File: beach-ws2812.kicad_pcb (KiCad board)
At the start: 4 copper layers, 260 x 120 mm, 24 parts, among them CON101 BARREL_JACK, P101 CONN_01X03, SW101 Pushbutton, SW102 Pushbutton, U101 STM32F103C(8-B)Tx, U102 LM1117-3.3, U103 MAX811, X101 8MHz

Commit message: Finished routing with only 1 random placed LED.
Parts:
- moved C201 7.02 mm to (25.0, 29.5), turned to 270 degrees
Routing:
- net LEDDATA: track 2.40 -> 240.8 mm, vias 1 -> 3
- net +3V3: track 120.6 -> 173.3 mm
- net GND: track 87.2 -> 128.5 mm, vias 11 -> 12
- net +5V: track 34.0 -> 41.4 mm, vias 1 -> 2
- net Net-(R101-Pad1): track 0.00 -> 3.90 mm
- net Net-(C102-Pad1): track 16.6 -> 17.7 mm

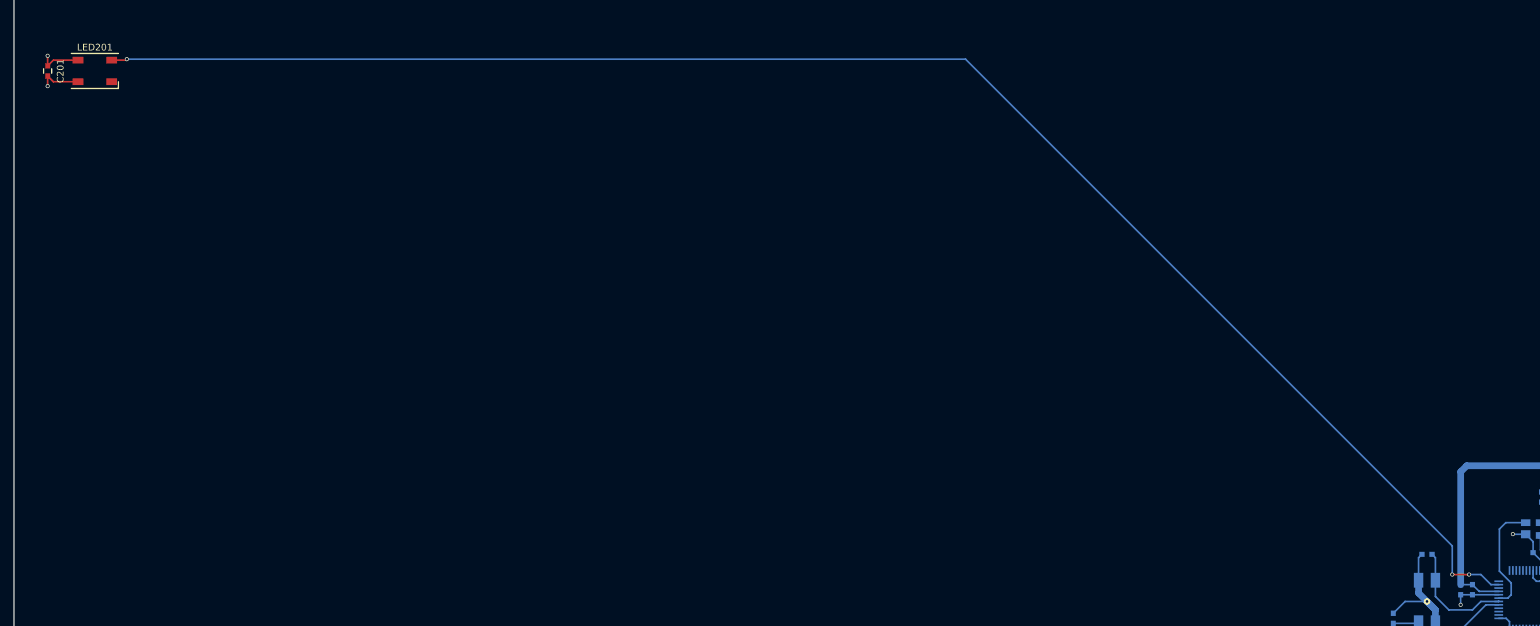
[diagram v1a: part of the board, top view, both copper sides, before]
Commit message: Routed to first LED final position.
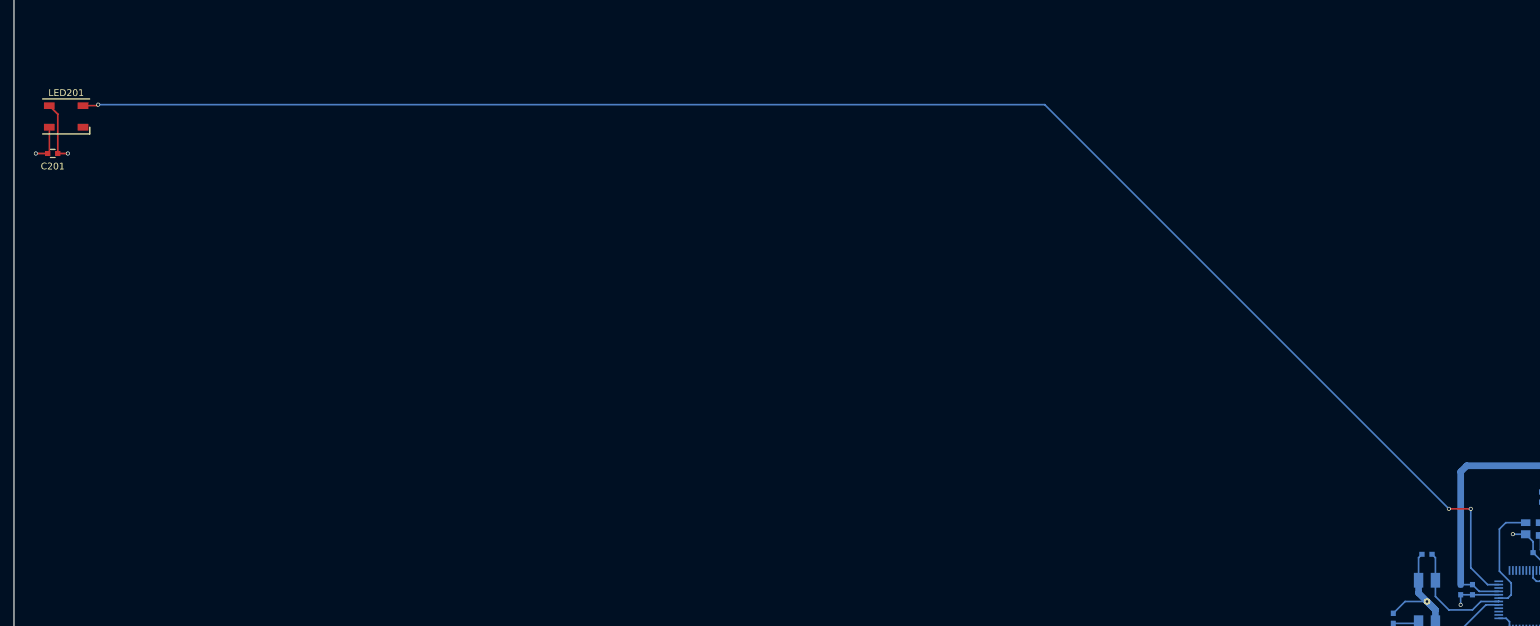
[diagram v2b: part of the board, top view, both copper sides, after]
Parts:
- added G***: LOGO, beach-ws2812:leds, F.Cu at (153.8, 78.5)
- moved C201 12.3 mm to (25.8, 41.8), turned to 180 degrees
- moved LED201 7.98 mm to (27.8, 36.2)
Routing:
- net LEDDATA: track 240.8 -> 244.9 mm
- net +5V: track 41.4 -> 43.9 mm
- net (no net): track 0.00 -> 2.00 mm
- net GND: track 128.5 -> 127.9 mm

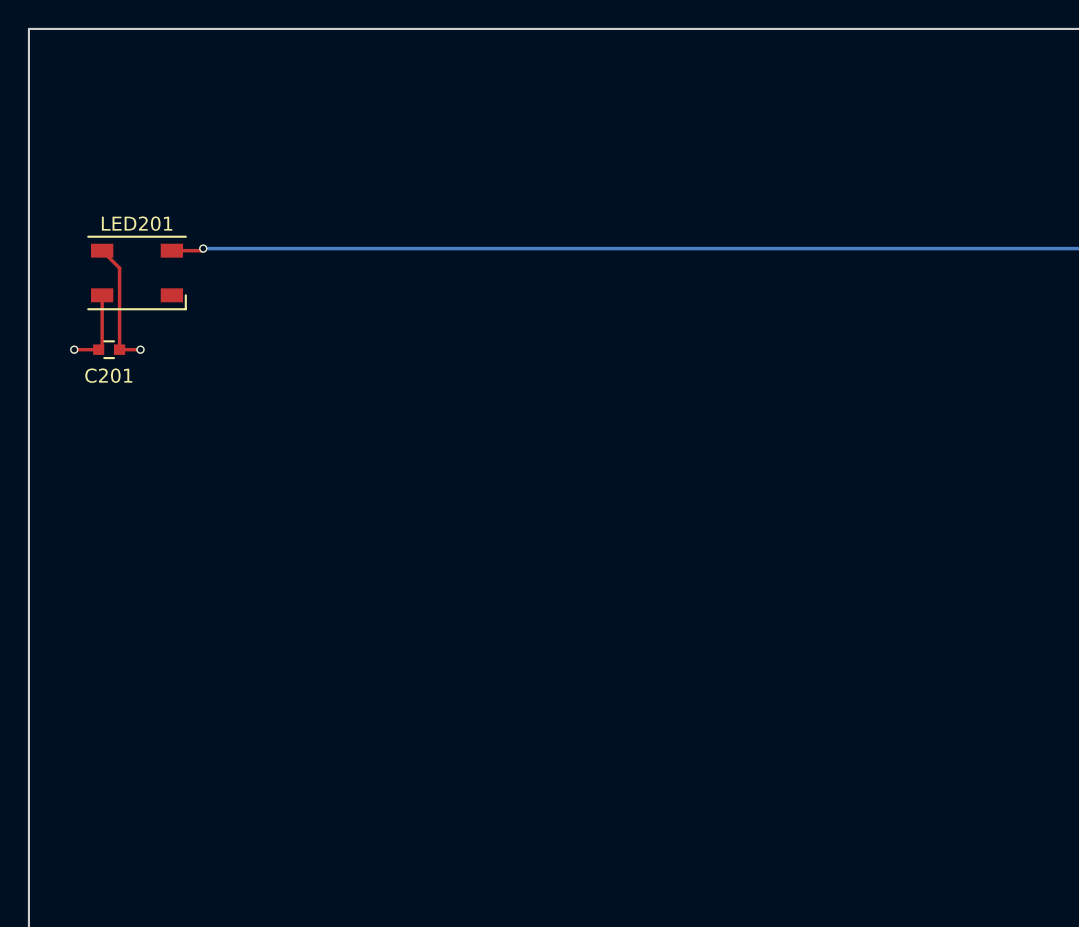
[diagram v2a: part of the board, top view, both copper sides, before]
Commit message: Now with 16 LEDs placed.
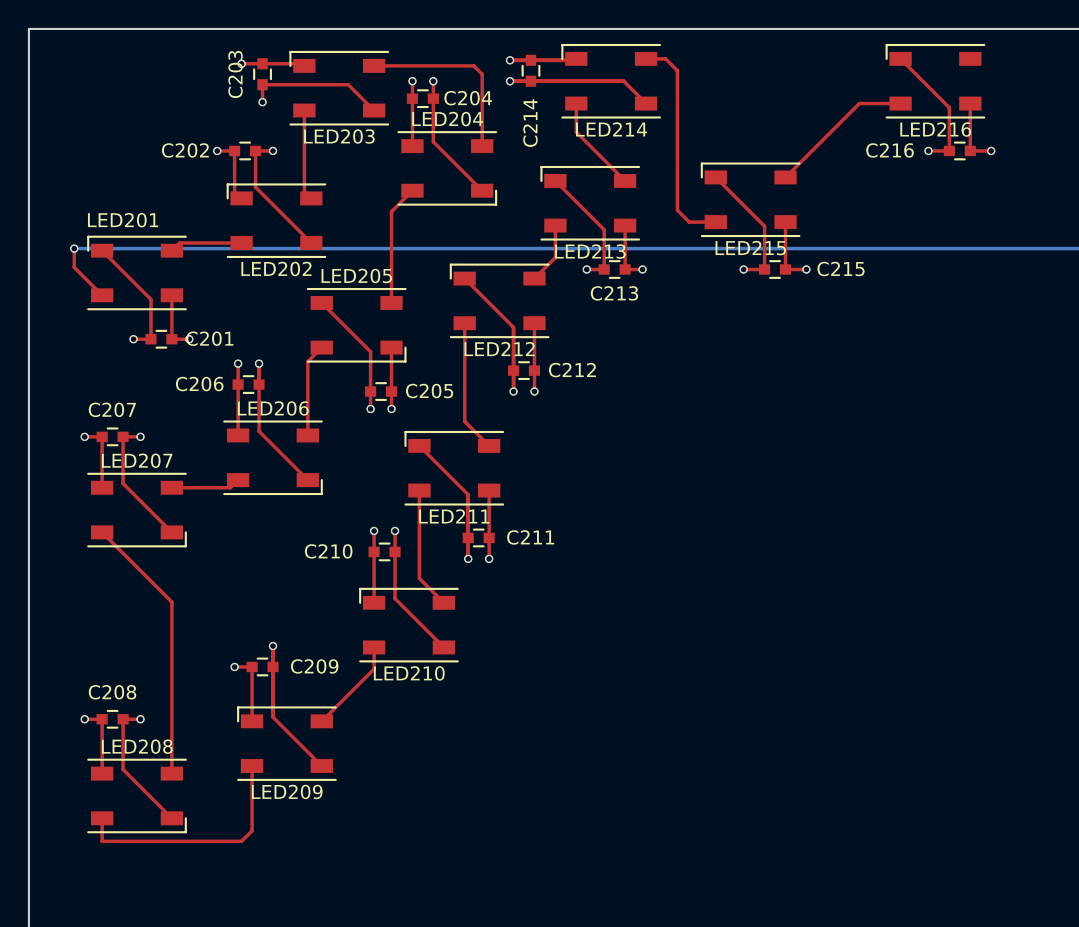
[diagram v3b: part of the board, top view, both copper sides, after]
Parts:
- added C202: 100nF, Capacitors_SMD:C_0603, F.Cu at (35.5, 27.5)
- added C203: 100nF, Capacitors_SMD:C_0603, F.Cu at (36.8, 22.0)
- added C204: 100nF, Capacitors_SMD:C_0603, F.Cu at (48.2, 23.8)
- added C205: 100nF, Capacitors_SMD:C_0603, F.Cu at (45.2, 44.8)
- added C206: 100nF, Capacitors_SMD:C_0603, F.Cu at (35.8, 44.2)
- added C207: 100nF, Capacitors_SMD:C_0603, F.Cu at (26.0, 48.0)
- added C208: 100nF, Capacitors_SMD:C_0603, F.Cu at (26.0, 68.2)
- added C209: 100nF, Capacitors_SMD:C_0603, F.Cu at (36.8, 64.5)
- added C210: 100nF, Capacitors_SMD:C_0603, F.Cu at (45.5, 56.2)
- added C211: 100nF, Capacitors_SMD:C_0603, F.Cu at (52.2, 55.2)
- added C212: 100nF, Capacitors_SMD:C_0603, F.Cu at (55.5, 43.2)
- added C213: 100nF, Capacitors_SMD:C_0603, F.Cu at (62.0, 36.0)
- added C214: 100nF, Capacitors_SMD:C_0603, F.Cu at (56.0, 21.8)
- added C215: 100nF, Capacitors_SMD:C_0603, F.Cu at (73.5, 36.0)
- added C216: 100nF, Capacitors_SMD:C_0603, F.Cu at (86.8, 27.5)
- added LED202: WS2812B, LEDs:LED_WS2812B-PLCC4, F.Cu at (37.8, 32.5)
- added LED203: WS2812B, LEDs:LED_WS2812B-PLCC4, F.Cu at (42.2, 23.0)
- added LED204: WS2812B, LEDs:LED_WS2812B-PLCC4, F.Cu at (50.0, 28.8)
- added LED205: WS2812B, LEDs:LED_WS2812B-PLCC4, F.Cu at (43.5, 40.0)
- added LED206: WS2812B, LEDs:LED_WS2812B-PLCC4, F.Cu at (37.5, 49.5)
- added LED207: WS2812B, LEDs:LED_WS2812B-PLCC4, F.Cu at (27.8, 53.2)
- added LED208: WS2812B, LEDs:LED_WS2812B-PLCC4, F.Cu at (27.8, 73.8)
- added LED209: WS2812B, LEDs:LED_WS2812B-PLCC4, F.Cu at (38.5, 70.0)
- added LED210: WS2812B, LEDs:LED_WS2812B-PLCC4, F.Cu at (47.2, 61.5)
- added LED211: WS2812B, LEDs:LED_WS2812B-PLCC4, F.Cu at (50.5, 50.2)
- added LED212: WS2812B, LEDs:LED_WS2812B-PLCC4, F.Cu at (53.8, 38.2)
- added LED213: WS2812B, LEDs:LED_WS2812B-PLCC4, F.Cu at (60.2, 31.2)
- added LED214: WS2812B, LEDs:LED_WS2812B-PLCC4, F.Cu at (61.8, 22.5)
- added LED215: WS2812B, LEDs:LED_WS2812B-PLCC4, F.Cu at (71.8, 31.0)
- added LED216: WS2812B, LEDs:LED_WS2812B-PLCC4, F.Cu at (85.0, 22.5)
- moved C201 3.82 mm to (29.5, 41.0)
- turned LED201 to 180 degrees
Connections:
- LED201 pad 2: GND -> Net-(LED201-Pad2)
- LED201 pad 3: Net-(LED201-Pad3) -> GND
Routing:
- net GND: track 127.9 -> 269.1 mm, vias 12 -> 27
- net +5V: track 43.9 -> 162.3 mm, vias 2 -> 17
- net Net-(LED207-Pad2): track 0.00 -> 19.4 mm
- net Net-(LED208-Pad2): track 0.00 -> 17.4 mm
- net Net-(LED214-Pad2): track 0.00 -> 15.7 mm
- net Net-(LED203-Pad2): track 0.00 -> 13.1 mm
- net LEDDATA: track 244.9 -> 256.0 mm
- net Net-(LED215-Pad2): track 0.00 -> 10.4 mm
- net Net-(LED211-Pad2): track 0.00 -> 9.52 mm
- net Net-(LED210-Pad2): track 0.00 -> 8.77 mm
- net Net-(LED204-Pad2): track 0.00 -> 8.67 mm
- net Net-(LED213-Pad2): track 0.00 -> 7.00 mm
- net Net-(LED209-Pad2): track 0.00 -> 6.85 mm
- net Net-(LED205-Pad2): track 0.00 -> 6.71 mm
- net Net-(LED202-Pad2): track 0.00 -> 6.51 mm
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
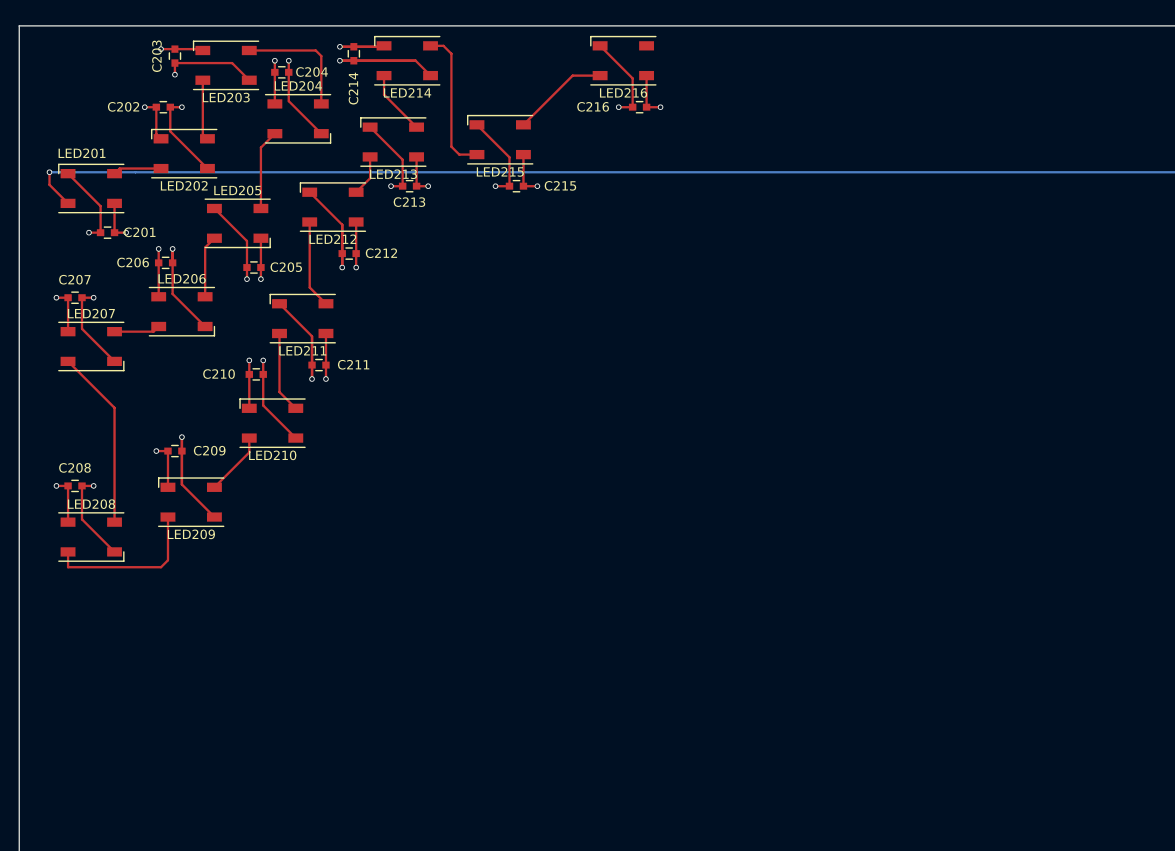
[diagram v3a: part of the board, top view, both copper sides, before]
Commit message: Routed 40 LEDs.
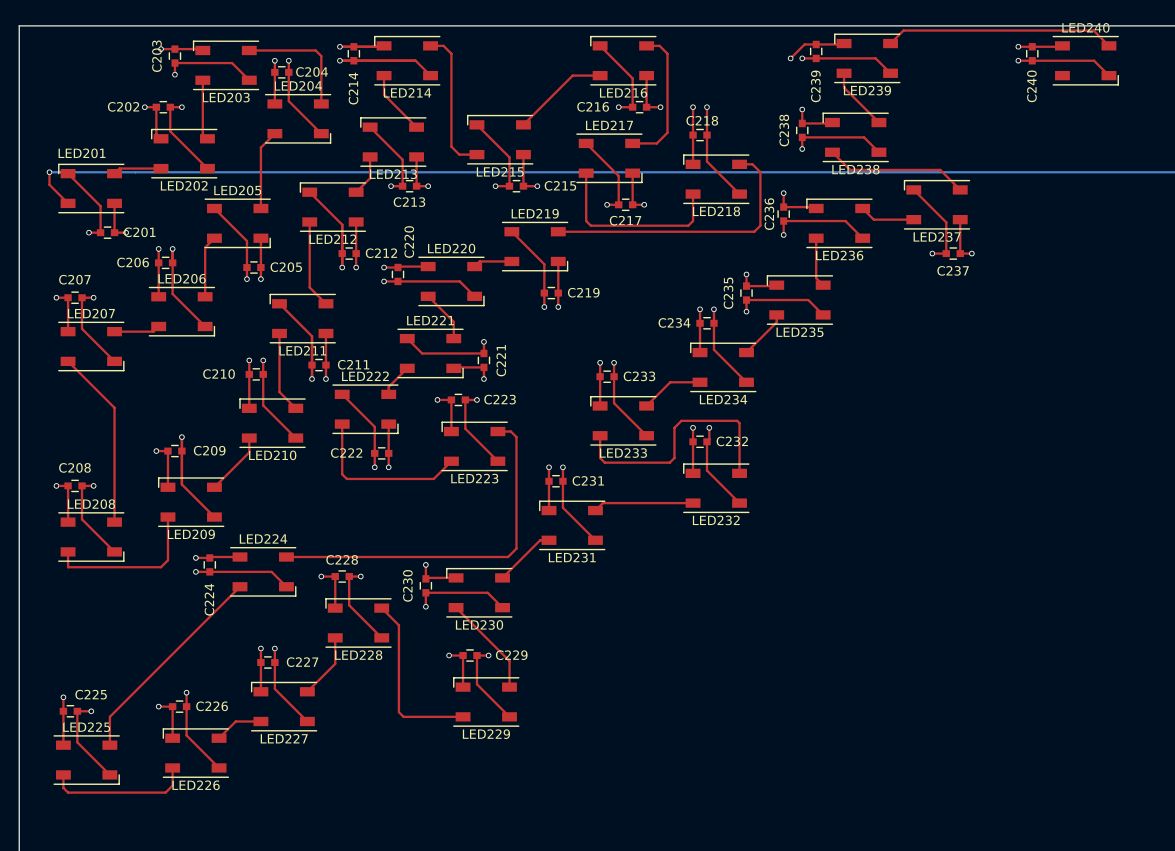
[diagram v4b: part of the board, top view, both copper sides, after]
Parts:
- added C217: 100nF, Capacitors_SMD:C_0603, F.Cu at (85.2, 38.0)
- added C218: 100nF, Capacitors_SMD:C_0603, F.Cu at (93.2, 30.5)
- added C219: 100nF, Capacitors_SMD:C_0603, F.Cu at (77.2, 47.5)
- added C220: 100nF, Capacitors_SMD:C_0603, F.Cu at (60.8, 45.5)
- added C221: 100nF, Capacitors_SMD:C_0603, F.Cu at (70.0, 54.8)
- added C222: 100nF, Capacitors_SMD:C_0603, F.Cu at (59.0, 64.8)
- added C223: 100nF, Capacitors_SMD:C_0603, F.Cu at (67.2, 59.0)
- added C224: 100nF, Capacitors_SMD:C_0603, F.Cu at (40.5, 76.8)
- added C225: 100nF, Capacitors_SMD:C_0603, F.Cu at (25.5, 92.5)
- added C226: 100nF, Capacitors_SMD:C_0603, F.Cu at (37.2, 92.0)
- added C227: 100nF, Capacitors_SMD:C_0603, F.Cu at (46.8, 87.2)
- added C228: 100nF, Capacitors_SMD:C_0603, F.Cu at (54.8, 78.0)
- added C229: 100nF, Capacitors_SMD:C_0603, F.Cu at (68.5, 86.5)
- added C230: 100nF, Capacitors_SMD:C_0603, F.Cu at (63.8, 79.0)
- added C231: 100nF, Capacitors_SMD:C_0603, F.Cu at (77.8, 67.8)
- added C232: 100nF, Capacitors_SMD:C_0603, F.Cu at (93.2, 63.5)
- added C233: 100nF, Capacitors_SMD:C_0603, F.Cu at (83.2, 56.5)
- added C234: 100nF, Capacitors_SMD:C_0603, F.Cu at (94.0, 50.8)
- added C235: 100nF, Capacitors_SMD:C_0603, F.Cu at (98.2, 47.5)
- added C236: 100nF, Capacitors_SMD:C_0603, F.Cu at (102.2, 39.0)
- added C237: 100nF, Capacitors_SMD:C_0603, F.Cu at (120.5, 43.2)
- added C238: 100nF, Capacitors_SMD:C_0603, F.Cu at (104.2, 30.0)
- added C239: 100nF, Capacitors_SMD:C_0603, F.Cu at (105.8, 21.5)
- added C240: 100nF, Capacitors_SMD:C_0603, F.Cu at (129.0, 21.8)
- added LED217: WS2812B, LEDs:LED_WS2812B-PLCC4, F.Cu at (83.5, 33.0)
- added LED218: WS2812B, LEDs:LED_WS2812B-PLCC4, F.Cu at (95.0, 35.2)
- added LED219: WS2812B, LEDs:LED_WS2812B-PLCC4, F.Cu at (75.5, 42.5)
- added LED220: WS2812B, LEDs:LED_WS2812B-PLCC4, F.Cu at (66.5, 46.2)
- added LED221: WS2812B, LEDs:LED_WS2812B-PLCC4, F.Cu at (64.2, 54.0)
- added LED222: WS2812B, LEDs:LED_WS2812B-PLCC4, F.Cu at (57.2, 60.0)
- added LED223: WS2812B, LEDs:LED_WS2812B-PLCC4, F.Cu at (69.0, 64.0)
- added LED224: WS2812B, LEDs:LED_WS2812B-PLCC4, F.Cu at (46.2, 77.5)
- added LED225: WS2812B, LEDs:LED_WS2812B-PLCC4, F.Cu at (27.2, 97.8)
- added LED226: WS2812B, LEDs:LED_WS2812B-PLCC4, F.Cu at (39.0, 97.0)
- added LED227: WS2812B, LEDs:LED_WS2812B-PLCC4, F.Cu at (48.5, 92.0)
- added LED228: WS2812B, LEDs:LED_WS2812B-PLCC4, F.Cu at (56.5, 83.0)
- added LED229: WS2812B, LEDs:LED_WS2812B-PLCC4, F.Cu at (70.2, 91.5)
- added LED230: WS2812B, LEDs:LED_WS2812B-PLCC4, F.Cu at (69.5, 79.8)
- added LED231: WS2812B, LEDs:LED_WS2812B-PLCC4, F.Cu at (79.5, 72.5)
- added LED232: WS2812B, LEDs:LED_WS2812B-PLCC4, F.Cu at (95.0, 68.5)
- added LED233: WS2812B, LEDs:LED_WS2812B-PLCC4, F.Cu at (85.0, 61.2)
- added LED234: WS2812B, LEDs:LED_WS2812B-PLCC4, F.Cu at (95.8, 55.5)
- added LED235: WS2812B, LEDs:LED_WS2812B-PLCC4, F.Cu at (104.0, 48.2)
- added LED236: WS2812B, LEDs:LED_WS2812B-PLCC4, F.Cu at (108.2, 40.0)
- added LED237: WS2812B, LEDs:LED_WS2812B-PLCC4, F.Cu at (118.8, 38.0)
- added LED238: WS2812B, LEDs:LED_WS2812B-PLCC4, F.Cu at (110.0, 30.8)
- added LED239: WS2812B, LEDs:LED_WS2812B-PLCC4, F.Cu at (111.2, 22.2)
- added LED240: WS2812B, LEDs:LED_WS2812B-PLCC4, F.Cu at (134.8, 22.5)
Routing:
- net +5V: track 162.3 -> 384.3 mm, vias 17 -> 41
- net GND: track 269.1 -> 425.8 mm, vias 27 -> 51
- net Net-(LED223-Pad2): track 0.00 -> 39.4 mm
- net Net-(LED218-Pad2): track 0.00 -> 30.5 mm
- net Net-(LED232-Pad2): track 0.00 -> 26.9 mm
- net Net-(LED239-Pad2): track 0.00 -> 24.8 mm
- net Net-(LED224-Pad2): track 0.00 -> 22.8 mm
- net Net-(LED217-Pad2): track 0.00 -> 20.0 mm
- net Net-(LED228-Pad2): track 0.00 -> 19.1 mm
- net Net-(LED222-Pad2): track 0.00 -> 18.1 mm
- net Net-(LED225-Pad2): track 0.00 -> 15.6 mm
- net Net-(LED237-Pad2): track 0.00 -> 15.4 mm
- net Net-(LED216-Pad2): track 0.00 -> 15.3 mm
- net Net-(LED229-Pad2): track 0.00 -> 10.9 mm
- net Net-(LED231-Pad2): track 0.00 -> 10.8 mm
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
